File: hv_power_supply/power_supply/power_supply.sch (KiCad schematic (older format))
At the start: 0 parts

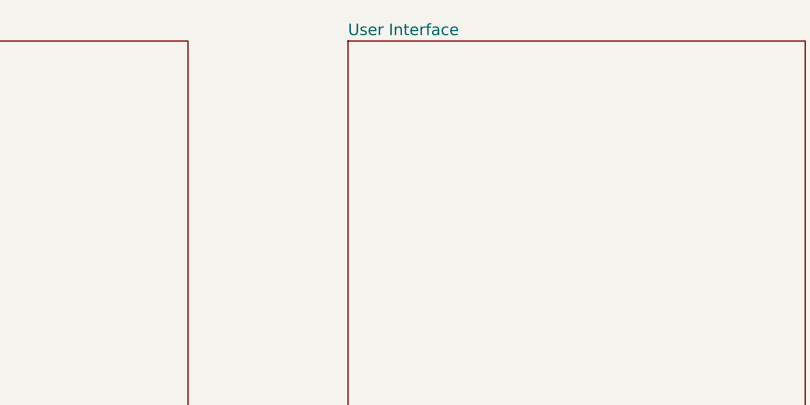
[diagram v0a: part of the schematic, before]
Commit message: add hierarchical label and edit UI schematic
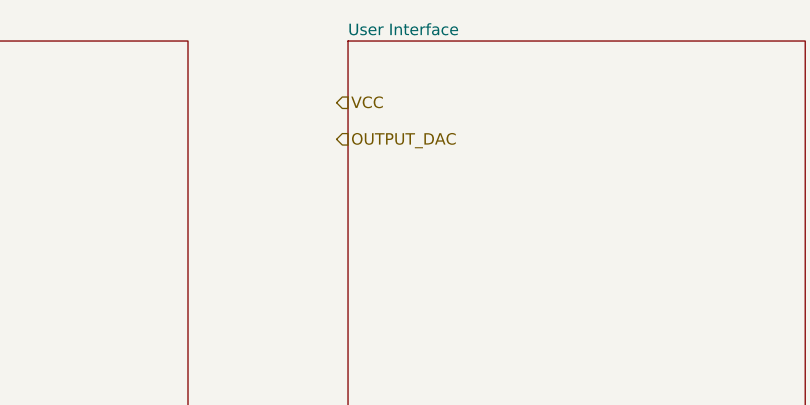
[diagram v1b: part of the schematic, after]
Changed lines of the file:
@@
 $Descr A4 11693 8268
 encoding utf-8
-Sheet 1 4
+Sheet 1 5
 Title ""
 Date ""
@@
 F1 "protections.sch" 50
 $EndSheet
+Text HLabel 6700 1820 2    50   Input ~ 0
+VCC
+Text HLabel 6700 1980 2    50   Input ~ 0
+OUTPUT_DAC
 $EndSCHEMATC

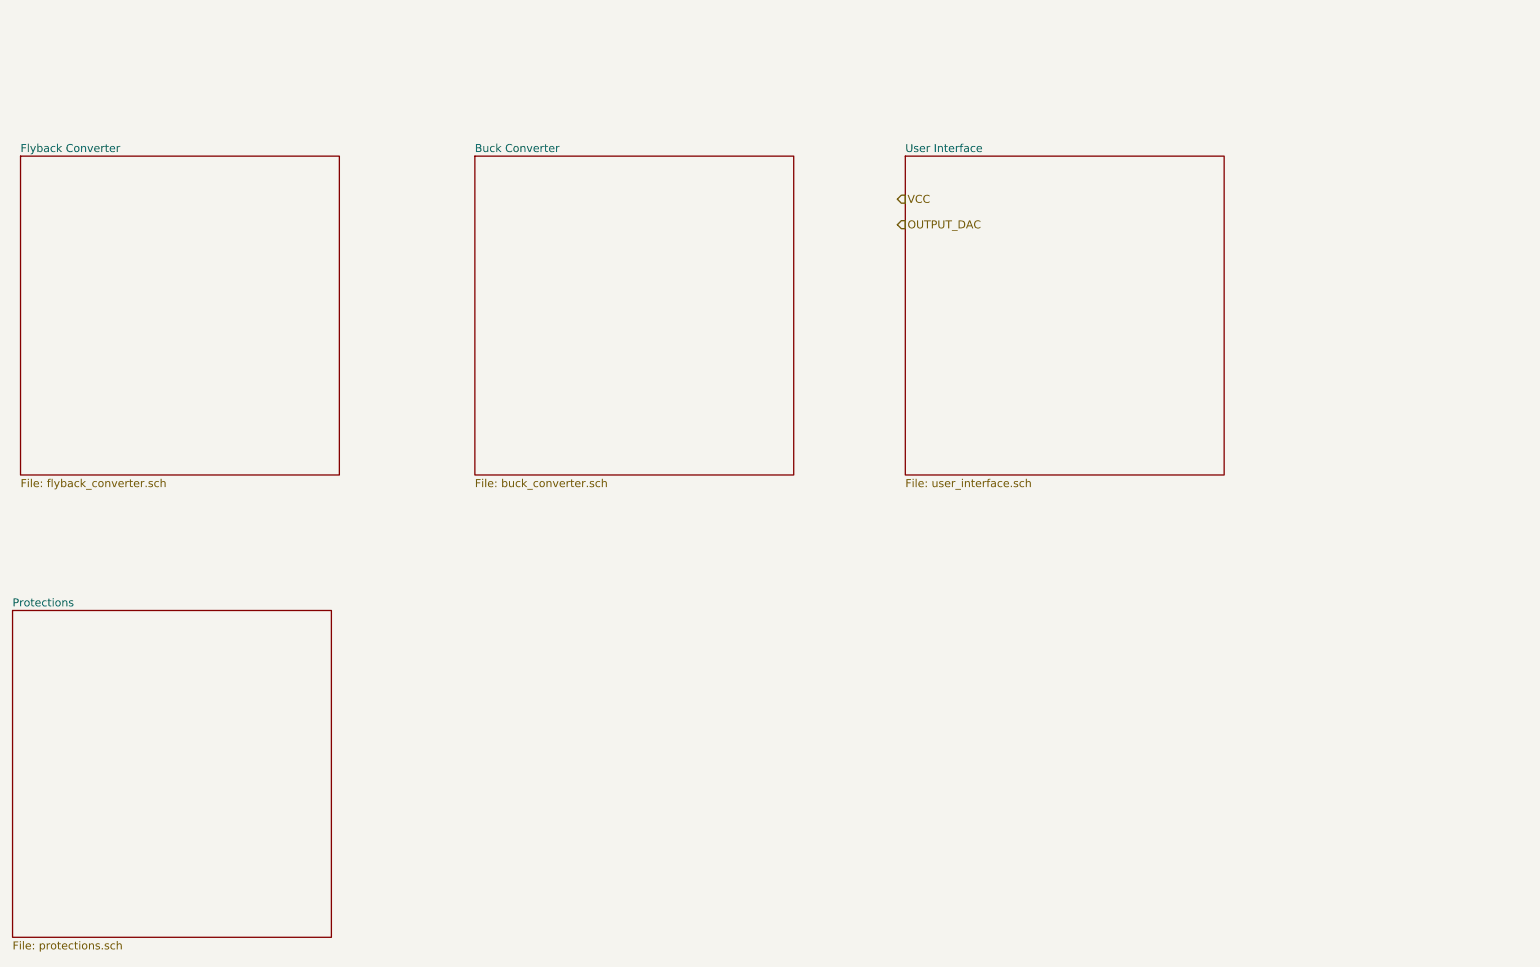
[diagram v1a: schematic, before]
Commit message: make schematic sheets talk to each other
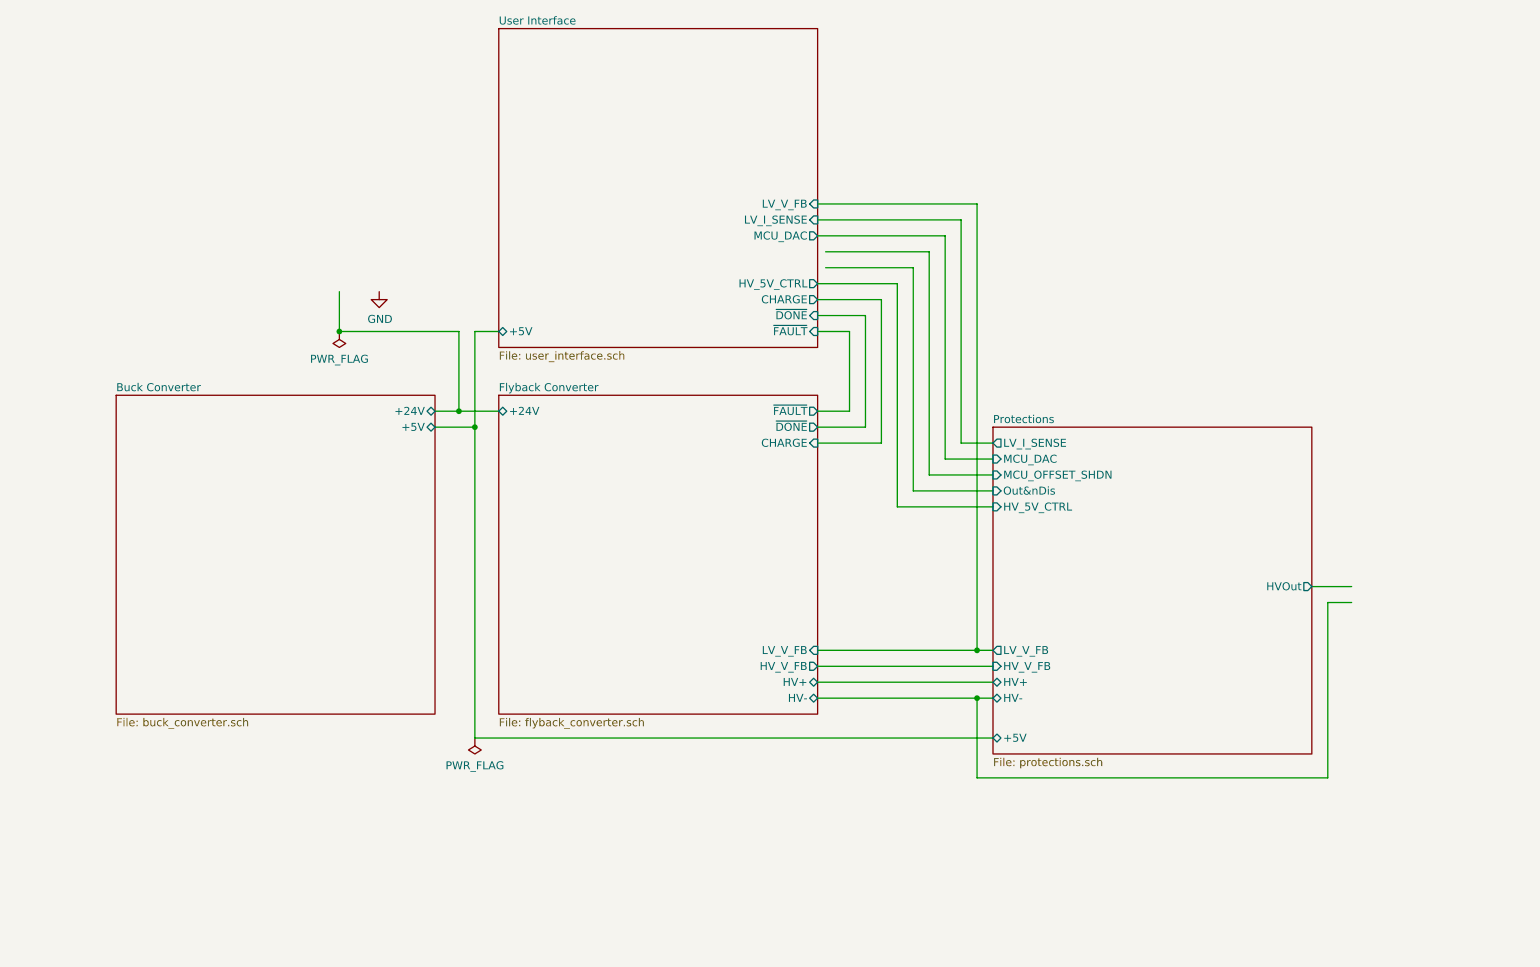
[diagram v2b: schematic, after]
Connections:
- net labels added: GND
- net labels removed: OUTPUT_DAC, VCC
- wire segments 0 -> 47
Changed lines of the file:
@@
 $EndDescr
 $Sheet
-S 1200 1550 2000 2000
+S 4200 3050 2000 2000
 U 5F8B2FE7
 F0 "Flyback Converter" 50
 F1 "flyback_converter.sch" 50
+F2 "HV+" B R 6200 4850 50
+F3 "HV-" B R 6200 4950 50
+F4 "HV_V_FB" O R 6200 4750 50
+F5 "~FAULT" O R 6200 3150 50
+F6 "~DONE" O R 6200 3250 50
+F7 "CHARGE" I R 6200 3350 50
+F8 "LV_V_FB" I R 6200 4650 50
+F9 "+24V" B L 4200 3150 50
 $EndSheet
 $Sheet
-S 4050 1550 2000 2000
+S 1800 3050 2000 2000
 U 5F8B3031
 F0 "Buck Converter" 50
 F1 "buck_converter.sch" 50
+F2 "+5V" B R 3800 3250 50
+F3 "+24V" B R 3800 3150 50
 $EndSheet
 $Sheet
-S 6750 1550 2000 2000
+S 7300 3250 2000 2050
+U 5F8B30A2
+F0 "Protections" 50
+F1 "protections.sch" 50
+F2 "Out&nDis" I L 7300 3650 50
+F3 "HV-" B L 7300 4950 50
+F4 "HV+" B L 7300 4850 50
+F5 "HVOut" O R 9300 4250 50
+F6 "LV_V_FB" O L 7300 4650 50
+F7 "+5V" B L 7300 5200 50
+F8 "LV_I_SENSE" O L 7300 3350 50
+F9 "MCU_DAC" I L 7300 3450 50
+F10 "MCU_OFFSET_SHDN" I L 7300 3550 50
+F11 "HV_5V_CTRL" I L 7300 3750 50
+F12 "HV_V_FB" I L 7300 4750 50
+$EndSheet
+$Sheet
+S 4200 750  2000 2000
 U 5F8B307F
 F0 "User Interface" 50
 F1 "user_interface.sch" 50
+F2 "+5V" B L 4200 2650 50
+F3 "LV_V_FB" I R 6200 1850 50
+F4 "LV_I_SENSE" I R 6200 1950 50
+F5 "MCU_DAC" O R 6200 2050 50
+F6 "HV_5V_CTRL" O R 6200 2350 50
+F7 "CHARGE" O R 6200 2450 50
+F8 "~FAULT" I R 6200 2650 50
+F9 "~DONE" I R 6200 2550 50
 $EndSheet
-$Sheet
-S 1150 4400 2000 2050
-U 5F8B30A2
-F0 "Protections" 50
-F1 "protections.sch" 50
-$EndSheet
-Text HLabel 6700 1820 2    50   Input ~ 0
-VCC
-Text HLabel 6700 1980 2    50   Input ~ 0
-OUTPUT_DAC
+Wire Wire Line
+	7200 4650 7300 4650
+Wire Wire Line
+	7300 3350 7100 3350
+Wire Wire Line
+	7100 3350 7100 1950
+Wire Wire Line
+	7300 3450 7000 3450
+Wire Wire Line
+	7300 3550 6900 3550
+Wire Wire Line
+	7300 3650 6800 3650
+Wire Wire Line
+	7300 3750 6700 3750
+Wire Wire Line
+	6200 3150 6400 3150
+Wire Wire Line
+	6400 3150 6400 2650
+Wire Wire Line
+	6200 3250 6500 3250
+Wire Wire Line
+	6500 3250 6500 2550
+Wire Wire Line
+	6200 3350 6600 3350
+Wire Wire Line
+	6600 3350 6600 2450
+Wire Wire Line
+	7300 5200 4050 5200
+Wire Wire Line
+	6700 2350 6700 3750
+Wire Wire Line
+	6250 2250 6800 2250
+Wire Wire Line
+	6250 2150 6900 2150
+Wire Wire Line
+	6200 4650 7200 4650
+Connection ~ 7200 4650
+Wire Wire Line
+	7200 4650 7200 1850
+Wire Wire Line
+	6200 4750 7300 4750
+Wire Wire Line
+	6200 4850 7300 4850
+Wire Wire Line
+	6200 4950 7200 4950
+Wire Wire Line
+	7000 3450 7000 2050
+Wire Wire Line
+	6800 3650 6800 2250
+Wire Wire Line
+	6900 3550 6900 2150
+Wire Wire Line
+	7200 4950 7200 5450
+Wire Wire Line
+	7200 5450 9400 5450
+Wire Wire Line
+	9400 5450 9400 4350
+Connection ~ 7200 4950
+Wire Wire Line
+	7200 4950 7300 4950
+Wire Wire Line
+	9400 4350 9550 4350
+Wire Wire Line
+	9300 4250 9550 4250
+Wire Wire Line
+	4050 2650 4200 2650
+Wire Wire Line
+	6200 1950 7100 1950
+Wire Wire Line
+	6200 1850 7200 1850
+Wire Wire Line
+	6200 2050 7000 2050
+Wire Wire Line
+	6200 2350 6700 2350
+Wire Wire Line
+	6200 2450 6600 2450
+Wire Wire Line
+	6200 2550 6500 2550
+Wire Wire Line
+	6200 2650 6400 2650
+Wire Wire Line
+	4050 2650 4050 3250
+Wire Wire Line
+	3800 3150 3950 3150
+Wire Wire Line
+	3800 3250 4050 3250
+Connection ~ 4050 3250
+Wire Wire Line
+	4050 3250 4050 5200
+Wire Wire Line
+	3950 3150 3950 2650
+Wire Wire Line
+	3950 2650 3200 2650
+Connection ~ 3950 3150
+Wire Wire Line
+	3950 3150 4200 3150
+$Comp
+L power:GND #PWR01
+U 1 1 607CC6CE
+P 3450 2400
+F 0 "#PWR01" H 3450 2150 50  0001 C CNN
+F 1 "GND" H 3455 2227 50  0000 C CNN
+F 2 "" H 3450 2400 50  0001 C CNN
+F 3 "" H 3450 2400 50  0001 C CNN
+	1    3450 2400
+	1    0    0    -1
+$EndComp
+Wire Wire Line
+	3200 2400 3200 2650
+$Comp
+L power:PWR_FLAG #FLG0101
+U 1 1 607D3A44
+P 3200 2650
+F 0 "#FLG0101" H 3200 2725 50  0001 C CNN
+F 1 "PWR_FLAG" H 3200 2823 50  0000 C CNN
+F 2 "" H 3200 2650 50  0001 C CNN
+F 3 "" H 3200 2650 50  0001 C CNN
+	1    3200 2650
+	-1   0    0    1
+$EndComp
+Connection ~ 3200 2650
+$Comp
+L power:PWR_FLAG #FLG0102
+U 1 1 605FBEF3
+P 4050 5200
+F 0 "#FLG0102" H 4050 5275 50  0001 C CNN
+F 1 "PWR_FLAG" H 4050 5373 50  0000 C CNN
+F 2 "" H 4050 5200 50  0001 C CNN
+F 3 "" H 4050 5200 50  0001 C CNN
+	1    4050 5200
+	-1   0    0    1
+$EndComp
 $EndSCHEMATC

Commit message: updated MCU pins
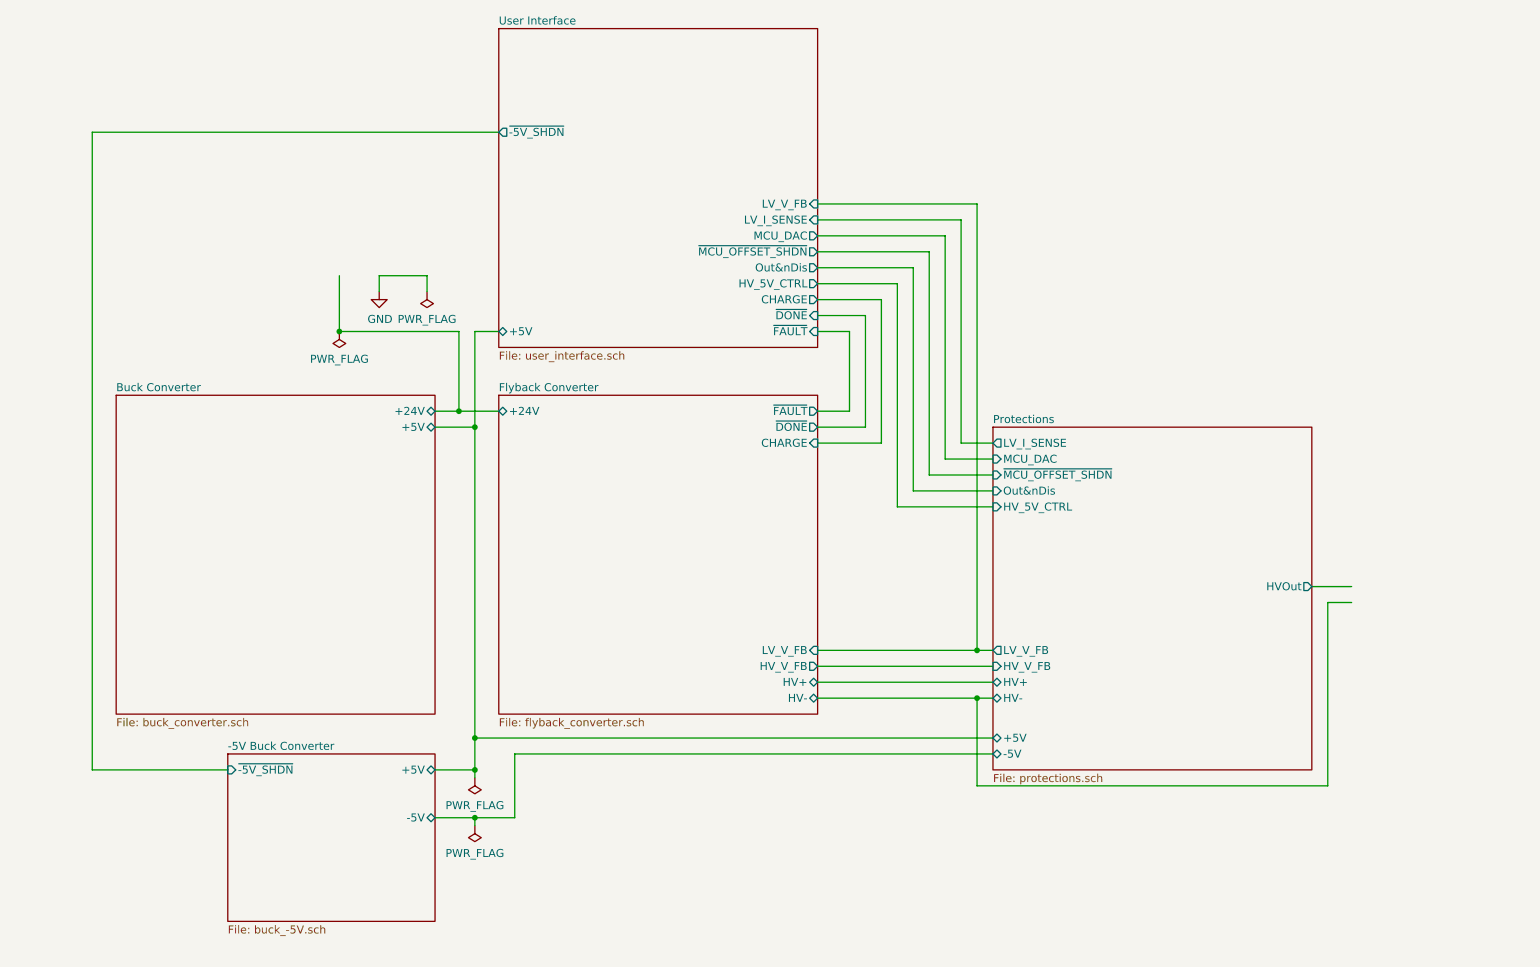
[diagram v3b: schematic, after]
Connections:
- wire segments 47 -> 61
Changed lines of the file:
@@
 $Descr A4 11693 8268
 encoding utf-8
-Sheet 1 5
+Sheet 1 6
 Title ""
 Date ""
@@
 $EndSheet
 $Sheet
-S 7300 3250 2000 2050
-U 5F8B30A2
-F0 "Protections" 50
-F1 "protections.sch" 50
-F2 "Out&nDis" I L 7300 3650 50
-F3 "HV-" B L 7300 4950 50
-F4 "HV+" B L 7300 4850 50
-F5 "HVOut" O R 9300 4250 50
-F6 "LV_V_FB" O L 7300 4650 50
-F7 "+5V" B L 7300 5200 50
-F8 "LV_I_SENSE" O L 7300 3350 50
-F9 "MCU_DAC" I L 7300 3450 50
-F10 "MCU_OFFSET_SHDN" I L 7300 3550 50
-F11 "HV_5V_CTRL" I L 7300 3750 50
-F12 "HV_V_FB" I L 7300 4750 50
-$EndSheet
-$Sheet
 S 4200 750  2000 2000
 U 5F8B307F
@@
 F8 "~FAULT" I R 6200 2650 50
 F9 "~DONE" I R 6200 2550 50
+F10 "~MCU_OFFSET_SHDN" O R 6200 2150 50
+F11 "Out&nDis" O R 6200 2250 50
+F12 "~-5V_SHDN" O L 4200 1400 50
 $EndSheet
 Wire Wire Line
@@
 Wire Wire Line
 	6700 2350 6700 3750
-Wire Wire Line
-	6250 2250 6800 2250
-Wire Wire Line
-	6250 2150 6900 2150
 Wire Wire Line
 	6200 4650 7200 4650
@@
 Wire Wire Line
 	6900 3550 6900 2150
-Wire Wire Line
-	7200 4950 7200 5450
-Wire Wire Line
-	7200 5450 9400 5450
-Wire Wire Line
-	9400 5450 9400 4350
 Connection ~ 7200 4950
 Wire Wire Line
@@
 	1    0    0    -1
 $EndComp
-Wire Wire Line
-	3200 2400 3200 2650
-$Comp
-L power:PWR_FLAG #FLG0101
+$Comp
+L power:PWR_FLAG #FLG01
 U 1 1 607D3A44
 P 3200 2650
-F 0 "#FLG0101" H 3200 2725 50  0001 C CNN
+F 0 "#FLG01" H 3200 2725 50  0001 C CNN
 F 1 "PWR_FLAG" H 3200 2823 50  0000 C CNN
 F 2 "" H 3200 2650 50  0001 C CNN
@@
 Connection ~ 3200 2650
 $Comp
-L power:PWR_FLAG #FLG0102
+L power:PWR_FLAG #FLG02
 U 1 1 605FBEF3
-P 4050 5200
-F 0 "#FLG0102" H 4050 5275 50  0001 C CNN
-F 1 "PWR_FLAG" H 4050 5373 50  0000 C CNN
-F 2 "" H 4050 5200 50  0001 C CNN
-F 3 "" H 4050 5200 50  0001 C CNN
-	1    4050 5200
-	-1   0    0    1
-$EndComp
+P 4050 5450
+F 0 "#FLG02" H 4050 5525 50  0001 C CNN
+F 1 "PWR_FLAG" H 4050 5623 50  0000 C CNN
+F 2 "" H 4050 5450 50  0001 C CNN
+F 3 "" H 4050 5450 50  0001 C CNN
+	1    4050 5450
+	-1   0    0    1
+$EndComp
+$Sheet
+S 2500 5300 1300 1050
+U 605F599C
+F0 "-5V Buck Converter" 50
+F1 "buck_-5V.sch" 50
+F2 "+5V" B R 3800 5400 50
+F3 "-5V" B R 3800 5700 50
+F4 "~-5V_SHDN" I L 2500 5400 50
+$EndSheet
+Wire Wire Line
+	4050 5200 4050 5400
+Connection ~ 4050 5200
+Wire Wire Line
+	3800 5400 4050 5400
+Connection ~ 4050 5400
+Wire Wire Line
+	4050 5400 4050 5450
+$Comp
+L power:PWR_FLAG #FLG03
+U 1 1 605FB304
+P 4050 5750
+F 0 "#FLG03" H 4050 5825 50  0001 C CNN
+F 1 "PWR_FLAG" H 4050 5923 50  0000 C CNN
+F 2 "" H 4050 5750 50  0001 C CNN
+F 3 "" H 4050 5750 50  0001 C CNN
+	1    4050 5750
+	-1   0    0    1
+$EndComp
+Wire Wire Line
+	3800 5700 4050 5700
+Wire Wire Line
+	4050 5700 4050 5750
+Wire Wire Line
+	4050 5700 4300 5700
+Connection ~ 4050 5700
+$Sheet
+S 7300 3250 2000 2150
+U 5F8B30A2
+F0 "Protections" 50
+F1 "protections.sch" 50
+F2 "Out&nDis" I L 7300 3650 50
+F3 "HV-" B L 7300 4950 50
+F4 "HV+" B L 7300 4850 50
+F5 "HVOut" O R 9300 4250 50
+F6 "LV_V_FB" O L 7300 4650 50
+F7 "+5V" B L 7300 5200 50
+F8 "LV_I_SENSE" O L 7300 3350 50
+F9 "MCU_DAC" I L 7300 3450 50
+F10 "HV_5V_CTRL" I L 7300 3750 50
+F11 "HV_V_FB" I L 7300 4750 50
+F12 "~MCU_OFFSET_SHDN" I L 7300 3550 50
+F13 "-5V" B L 7300 5300 50
+$EndSheet
+Wire Wire Line
+	7200 5500 9400 5500
+Wire Wire Line
+	7200 4950 7200 5500
+Wire Wire Line
+	9400 4350 9400 5500
+Wire Wire Line
+	4300 5700 4300 5300
+Wire Wire Line
+	4300 5300 7300 5300
+$Comp
+L power:PWR_FLAG #FLG0101
+U 1 1 6063E536
+P 3750 2400
+F 0 "#FLG0101" H 3750 2475 50  0001 C CNN
+F 1 "PWR_FLAG" H 3750 2573 50  0000 C CNN
+F 2 "" H 3750 2400 50  0001 C CNN
+F 3 "" H 3750 2400 50  0001 C CNN
+	1    3750 2400
+	-1   0    0    1
+$EndComp
+Wire Wire Line
+	3450 2400 3450 2300
+Wire Wire Line
+	3450 2300 3750 2300
+Wire Wire Line
+	3750 2300 3750 2400
+Wire Wire Line
+	3200 2300 3200 2650
+Wire Wire Line
+	6200 2250 6800 2250
+Wire Wire Line
+	6200 2150 6900 2150
+Wire Wire Line
+	2500 5400 1650 5400
+Wire Wire Line
+	1650 5400 1650 1400
+Wire Wire Line
+	1650 1400 4200 1400
 $EndSCHEMATC
